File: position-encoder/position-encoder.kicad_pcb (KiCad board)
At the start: 2 copper layers, 73.7 x 43.2 mm, 9 parts, among them J1 Conn_01x04_Male, U1 TLE4905L, U2 TLE4905L

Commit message: Use proper mounting holes
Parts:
- added REF**: MountingHole_2.7mm_M2.5_ISO14580_Pad, MountingHole:MountingHole_2.7mm_M2.5_ISO14580_Pad, F.Cu at (132.1, 197.5)
- added REF**: MountingHole_2.7mm_M2.5_ISO14580_Pad, MountingHole:MountingHole_2.7mm_M2.5_ISO14580_Pad, F.Cu at (132.1, 170.8)
- added REF**: MountingHole_2.7mm_M2.5_ISO14580_Pad, MountingHole:MountingHole_2.7mm_M2.5_ISO14580_Pad, F.Cu at (78.1, 166.4)
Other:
- outline, holes or cut-outs redrawn

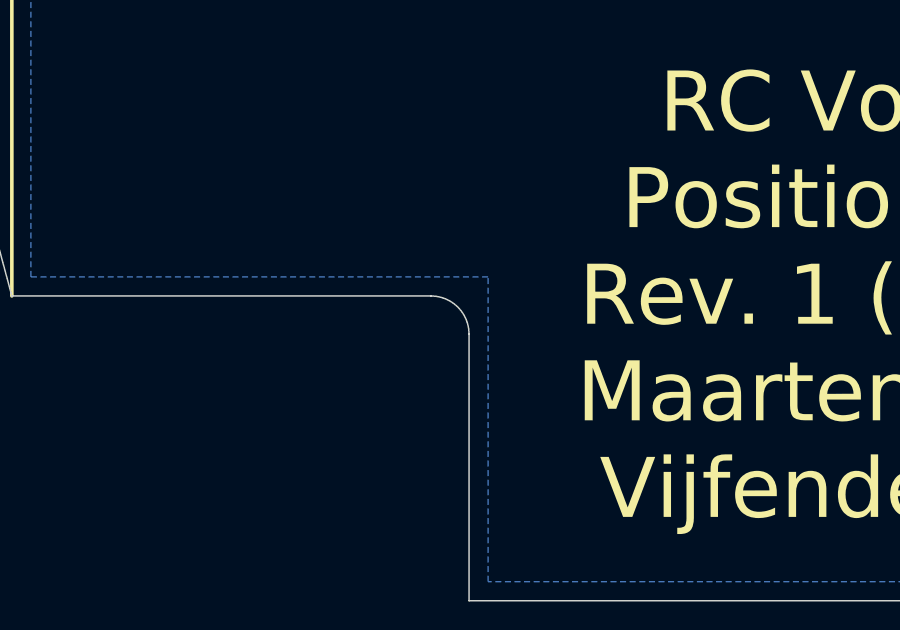
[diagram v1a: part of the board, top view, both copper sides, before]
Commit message: Update position encoder to KiCad 6.0
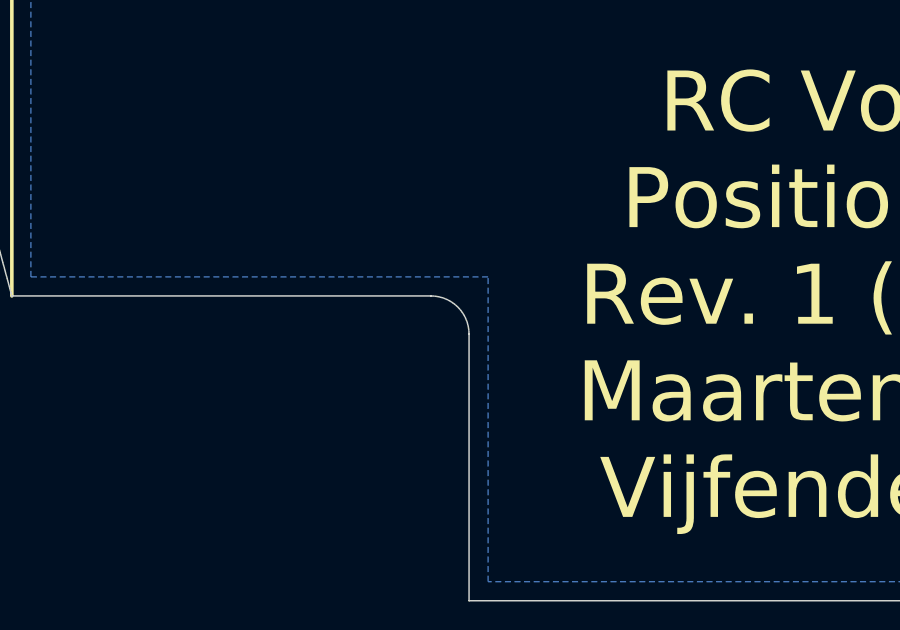
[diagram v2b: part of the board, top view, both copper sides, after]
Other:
- net class Default removed
- net class Power removed
- net class Signal removed
